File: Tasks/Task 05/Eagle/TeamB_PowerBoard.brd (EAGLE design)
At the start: 100.3 x 58.4 mm, 37 parts

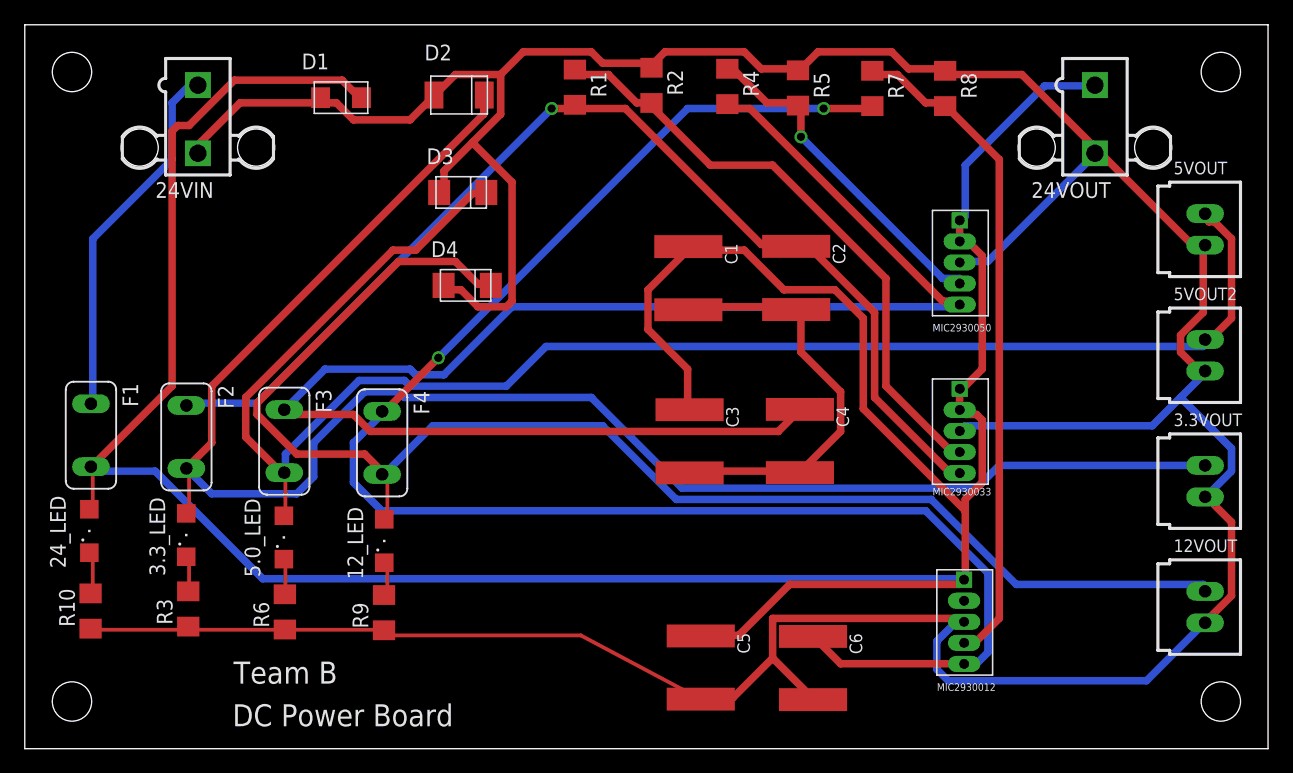
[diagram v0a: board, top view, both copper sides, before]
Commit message: Added submission files and cleaned up folders
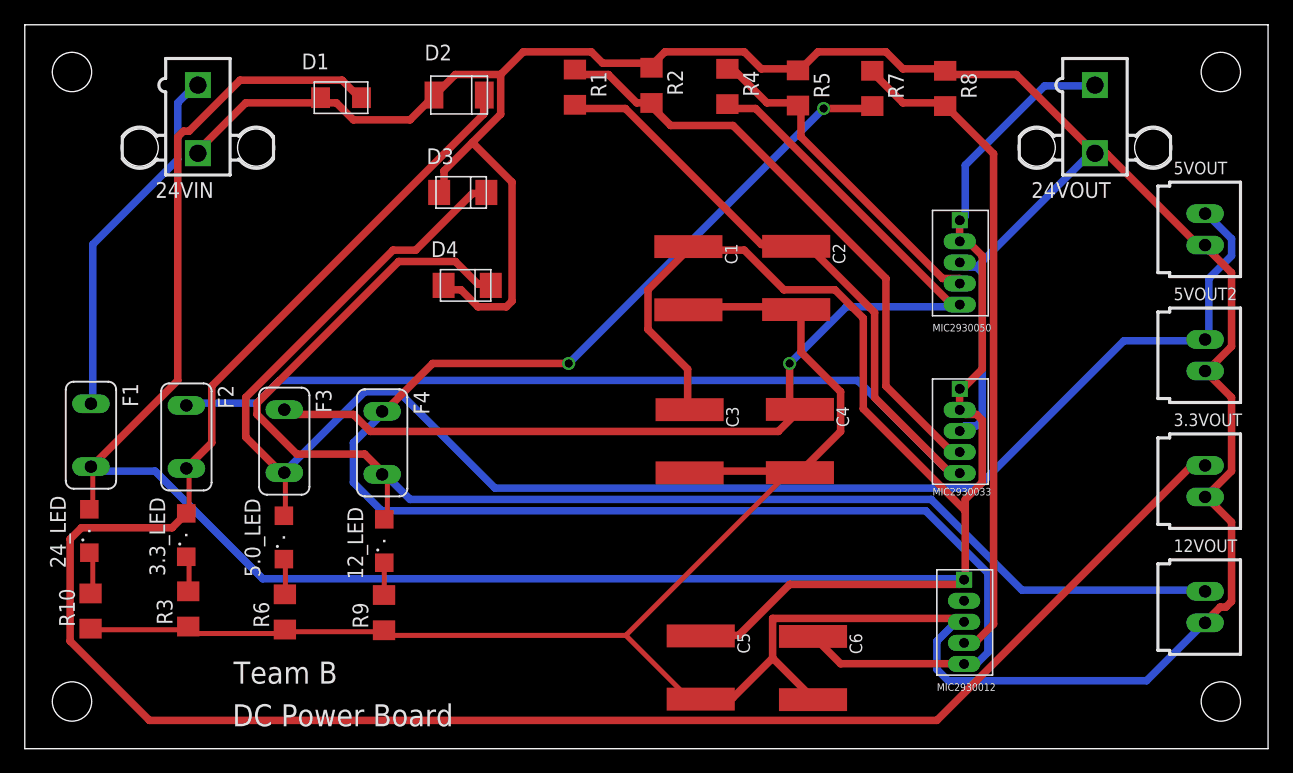
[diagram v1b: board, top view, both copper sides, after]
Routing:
- net N$7: track 127.3 -> 88.8 mm, vias 0 -> 1
- net N$9: track 136.2 -> 165.4 mm
- net N$5: track 89.0 -> 113.9 mm, vias 1 -> 0
- net GND: track 345.8 -> 360.4 mm
- net N$4: track 130.3 -> 134.8 mm
- net N$6: track 115.6 -> 112.1 mm
- net VCC: track 30.1 -> 29.4 mm
- net N$1: track 251.0 -> 250.3 mm
- net N$13: vias 1 -> 0
